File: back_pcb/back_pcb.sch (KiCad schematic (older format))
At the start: 90 parts, among them J1 Conn_01x12, P2 EXPANSION_BOTTOM, P3 EXPANSION_TOP, P4 AUDIO_CONN, P6 ATMEGA_HEADER, P7 EXPANSION_BOTTOM2, P8 JST, P9 USB_A, Q1 IRLML6401, Q2 IRLML6401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

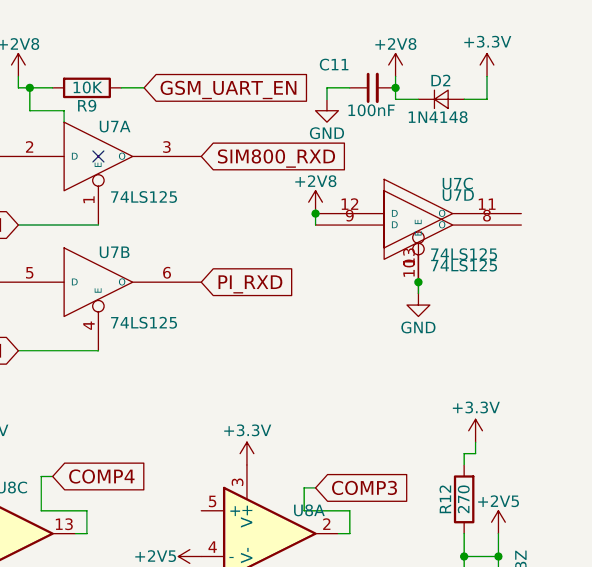
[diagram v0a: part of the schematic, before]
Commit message: Added a 10K resistor pulling up the buffer's unused gate ENs, cleaned up silkscreen
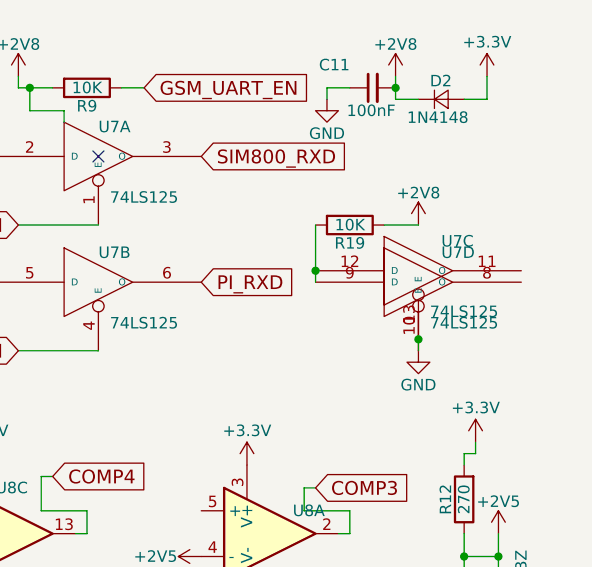
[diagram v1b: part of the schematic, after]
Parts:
- added R19: 10K, common-footprints:R_0805_10K_HandSoldering, symbol R
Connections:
- wire segments 152 -> 153
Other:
- moved on the sheet: U7C, U7D

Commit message: Adjusted JST footprint, connected USB shield to ground, moved some traces and silkscreen labels
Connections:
- no-connect marks 20 -> 19
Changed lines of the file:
@@
 	0    1    1    0
 $EndComp
-NoConn ~ 10850 5350
 $Comp
 L +5V #PWR98
@@
 Text GLabel 6650 6200 0    60   Input ~ 0
 BAT_IN+
-Text Notes 10150 5550 0    60   ~ 0
+Text Notes 10000 5550 0    60   ~ 0
 Full-sized USB \nfemale socket
 $Comp
@@
 Wire Wire Line
 	10500 2700 10650 2700
+$Comp
+L GND #PWR?
+U 1 1 5A8EDCBB
+P 10850 5350
+F 0 "#PWR?" H 10850 5100 50  0001 C CNN
+F 1 "GND" H 10850 5200 50  0000 C CNN
+F 2 "" H 10850 5350 50  0000 C CNN
+F 3 "" H 10850 5350 50  0000 C CNN
+	1    10850 5350
+	1    0    0    -1
+$EndComp
 $EndSCHEMATC

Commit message: Made schematic prettier, fixed the DC-DC FET
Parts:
- D4: value D_Zener -> 5V1
- W1, W4: value TEST_1P -> TXD
- W10: value TEST_1P -> ARX
- W13: value TEST_1P -> ARG
- W14: value TEST_1P -> GND
- W2, W5: value TEST_1P -> RXD
- W29: value TEST_1P -> ADC
- W3: value TEST_1P -> Pi_RST
- W9: value TEST_1P -> ATX
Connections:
- wire segments 153 -> 146
- no-connect marks 19 -> 21
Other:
- note added: "2.6-2.8V for\nthe GSM UART\nbuffer"
- note added: "5050 RGB LED, to be used as a\nflashlight and a notification LED"
- note added: "A TL431-based\nvoltage reference,\nto be used by the\ncomparator."
- note added: "An EEPROM\nfor the hardware version\nidentification, to be programmed\nwith the board version information"
- note added: "Comparators that detect charger\ninput or DC-DC output undervoltage\nThis version will detect back board\noverheating, too"
- note added: "Has two functions:\n1. level-shifting the GSM UART\n2. disabling the GSM UART from\nthe Pi UART until it's needed"
- note added: "Small headers with I2C, 3.3V,\n+5V, one GPIO, VIN and ADC. \nCan be useful for small analog and I2C\nsensors, as well as a dock station port."
- note added: "The UART buffer,\nbased on 74HC125 IC"
- note added: "Unused gates\nof 74HC125"
- note removed: "Small headers with I2C, 3.3V,\n+5V, one GPIO, VIN and ADC. \nCan be useful for small \nanalog and I2C sensors."
- moved on the sheet: C1, C10, C11, C2, C25, C7, D2, D3, D4, JP11, JP12, JP8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

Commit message: Back board changes
Changing 5-pin header footprint to match the RPi 5-header group
Moving the hardware ID EEPROM to I2C0 (ID_SD and ID_SC) pins
Adding pullup on the other I2C pin, as it's required per Pi HAT EEPROM
schematic
Removed TV_OUT pin from Pi Zero footprint
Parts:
- added R20: 10K, common-footprints:R_0805_10K_HandSoldering, symbol R
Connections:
- net labels added: ID_SD
- wire segments 146 -> 148
- no-connect marks 21 -> 20
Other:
- moved on the sheet: R11
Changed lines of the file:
@@
 NoConn ~ 2450 6200
 NoConn ~ 2450 6500
-NoConn ~ 950  4700
 $Comp
 L GND #PWR016
@@
 Text Notes 8950 5950 0    60   ~ 0
 Header with 2 GPIOs\nfor IR receiver \nor transmitter\n(or something else)
-Text GLabel 6600 6900 0    60   Input ~ 0
+Text GLabel 6600 7000 0    60   Input ~ 0
 SCL
 $Comp
 L GND #PWR025
 U 1 1 588A4E65
-P 6600 7100
-F 0 "#PWR025" H 6600 6850 50  0001 C CNN
-F 1 "GND" V 6600 6900 50  0000 C CNN
-F 2 "" H 6600 7100 50  0000 C CNN
-F 3 "" H 6600 7100 50  0000 C CNN
-	1    6600 7100
+P 6600 7200
+F 0 "#PWR025" H 6600 6950 50  0001 C CNN
+F 1 "GND" V 6600 7000 50  0000 C CNN
+F 2 "" H 6600 7200 50  0000 C CNN
+F 3 "" H 6600 7200 50  0000 C CNN
+	1    6600 7200
 	0    1    1    0
 $EndComp
 Text GLabel 5000 6900 2    60   Input ~ 0
 ATMEGA_ADC
-Text GLabel 6600 7000 0    60   Input ~ 0
+Text GLabel 6600 6900 0    60   Input ~ 0
 SDA
 Text Notes 4750 7450 0    60   ~ 0
@@
 	1    0    0    -1
 $EndComp
-Text GLabel 6850 1050 0    60   Input ~ 0
+Text GLabel 6600 1050 0    60   Input ~ 0
 MCP_INT
 $Comp
 L R R11
 U 1 1 58914037
-P 6850 800
-F 0 "R11" V 6930 800 50  0000 C CNN
-F 1 "10K" V 6850 800 50  0000 C CNN
-F 2 "common-footprints:R_0805_10K_HandSoldering" V 6780 800 50  0001 C CNN
-F 3 "" H 6850 800 50  0000 C CNN
-	1    6850 800
+P 6600 800
+F 0 "R11" V 6680 800 50  0000 C CNN
+F 1 "10K" V 6600 800 50  0000 C CNN
+F 2 "common-footprints:R_0805_10K_HandSoldering" V 6530 800 50  0001 C CNN
+F 3 "" H 6600 800 50  0000 C CNN
+	1    6600 800
 	1    0    0    -1
 $EndComp
@@
 	1    0    0    -1
 $EndComp
-Text GLabel 6600 6800 0    60   Input ~ 0
+Text GLabel 6600 7100 0    60   Input ~ 0
 BH_GPIO_1
 Text GLabel 2950 5450 2    60   Input ~ 0
@@
 L +3.3VA #PWR062
 U 1 1 5A853C54
-P 6600 7200
-F 0 "#PWR062" H 6600 7050 50  0001 C CNN
-F 1 "+3.3VA" V 6600 7450 50  0000 C CNN
-F 2 "" H 6600 7200 50  0001 C CNN
-F 3 "" H 6600 7200 50  0001 C CNN
-	1    6600 7200
+P 6600 6800
+F 0 "#PWR062" H 6600 6650 50  0001 C CNN
+F 1 "+3.3VA" V 6600 7050 50  0000 C CNN
+F 2 "" H 6600 6800 50  0001 C CNN
+F 3 "" H 6600 6800 50  0001 C CNN
+	1    6600 6800
 	0    -1   -1   0
 $EndComp
@@
 L +3.3VA #PWR064
 U 1 1 5A856D5E
-P 6850 650
-F 0 "#PWR064" H 6850 500 50  0001 C CNN
-F 1 "+3.3VA" H 6650 750 50  0000 C CNN
-F 2 "" H 6850 650 50  0001 C CNN
-F 3 "" H 6850 650 50  0001 C CNN
-	1    6850 650
+P 6600 650
+F 0 "#PWR064" H 6600 500 50  0001 C CNN
+F 1 "+3.3VA" H 6400 750 50  0000 C CNN
+F 2 "" H 6600 650 50  0001 C CNN
+F 3 "" H 6600 650 50  0001 C CNN
+	1    6600 650
 	1    0    0    -1
 $EndComp
@@
 L +3.3V #PWR073
 U 1 1 5A8624E1
-P 8600 1100
-F 0 "#PWR073" H 8600 950 50  0001 C CNN
-F 1 "+3.3V" H 8600 1250 50  0000 C CNN
-F 2 "" H 8600 1100 50  0000 C CNN
-F 3 "" H 8600 1100 50  0000 C CNN
-	1    8600 1100
-	1    0    0    -1
-$EndComp
-Text GLabel 8250 950  2    60   Input ~ 0
-SDA
-Text GLabel 8250 1050 2    60   Input ~ 0
-SCL
+P 8650 1200
+F 0 "#PWR073" H 8650 1050 50  0001 C CNN
+F 1 "+3.3V" H 8650 1350 50  0000 C CNN
+F 2 "" H 8650 1200 50  0000 C CNN
+F 3 "" H 8650 1200 50  0000 C CNN
+	1    8650 1200
+	-1   0    0    1
+$EndComp
 $Comp
 L GND #PWR074
@@
 	8250 1150 8300 1150
 Wire Wire Line
-	8600 1150 8600 1100
-Wire Wire Line
 	8250 1150 8250 1250
 Connection ~ 8250 1150
@@
 5050 RGB LED, to be used as a\nflashlight and a notification LED
 Wire Wire Line
-	6850 1050 6850 950
+	6600 1050 6600 950
 Wire Wire Line
 	10550 700  10550 750
@@
 Text Notes 10000 3650 0    60   ~ 0
 A TL431-based\nvoltage reference,\nto be used by the\ncomparator.
+Text GLabel 8250 1050 2    60   Input ~ 0
+MCP_INT
+Text GLabel 950  4700 0    60   Input ~ 0
+ID_SD
+Text GLabel 8250 950  2    60   Input ~ 0
+ID_SD
+Wire Wire Line
+	8600 1150 8650 1150
+Wire Wire Line
+	8650 1150 8650 1200
+$Comp
+L R R20
+U 1 1 5AA73F34
+P 6950 800
+F 0 "R20" V 7030 800 50  0000 C CNN
+F 1 "10K" V 6950 800 50  0000 C CNN
+F 2 "common-footprints:R_0805_10K_HandSoldering" V 6880 800 50  0001 C CNN
+F 3 "" H 6950 800 50  0000 C CNN
+	1    6950 800
+	1    0    0    -1
+$EndComp
+$Comp
+L +3.3VA #PWR0110
+U 1 1 5AA7406E
+P 6950 650
+F 0 "#PWR0110" H 6950 500 50  0001 C CNN
+F 1 "+3.3VA" H 6750 750 50  0000 C CNN
+F 2 "" H 6950 650 50  0001 C CNN
+F 3 "" H 6950 650 50  0001 C CNN
+	1    6950 650
+	1    0    0    -1
+$EndComp
+Text GLabel 6950 1050 0    60   Input ~ 0
+ID_SD
+Wire Wire Line
+	6950 1050 6950 950
 $EndSCHEMATC

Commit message: Removed MCP23017 addr jumpers, added fiducials, specified EEPROM model, added power-button-sense circuit, removed battery capacitor
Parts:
- removed C3: 100uF, Capacitors_Tantalum_SMD:CP_Tantalum_Case-B_EIA-3528-21_Hand, symbol C_Small
- removed JP3: A0, common-footprints:GS3_SMALL, symbol JUMPER3
- removed JP4: A1, common-footprints:GS3_SMALL, symbol JUMPER3
- removed JP6: A2, common-footprints:GS3_SMALL, symbol JUMPER3
- added D6: 1N4148, common-footprints:1N4148-D_MiniMELF_Handsoldering, symbol D_Small
- added R21, R22: 270, Resistors_SMD:R_0603_HandSoldering, symbol R
- added R23: 10K, common-footprints:R_0805_10K_HandSoldering, symbol R
- added TP1: FID1, Fiducials:Fiducial_1mm_Dia_2mm_Outer, symbol TEST
- added TP2: FID2, Fiducials:Fiducial_1mm_Dia_2mm_Outer, symbol TEST
- added TP3: FID3, Fiducials:Fiducial_1mm_Dia_2mm_Outer, symbol TEST
- added TP4: FID4, Fiducials:Fiducial_1mm_Dia_2mm_Outer, symbol TEST
- added TP5: FID5, Fiducials:Fiducial_1mm_Dia_2mm_Outer, symbol TEST
- added TP6: FID6, Fiducials:Fiducial_1mm_Dia_2mm_Outer, symbol TEST
- added TP7: FID7, Fiducials:Fiducial_1mm_Dia_2mm_Outer, symbol TEST
- added TP8: FID8, Fiducials:Fiducial_1mm_Dia_2mm_Outer, symbol TEST
- U5: value 24LC16 -> 24C32
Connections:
- wire segments 148 -> 146
- no-connect marks 20 -> 28
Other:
- note added: "JST-PH 2-pin\nbattery connector"
- note removed: "The address pins are \ninterconnected for a default \naddress (tracks can be cut \nand jumpered for custom \naddress)"
- moved on the sheet: P8, R4, U4

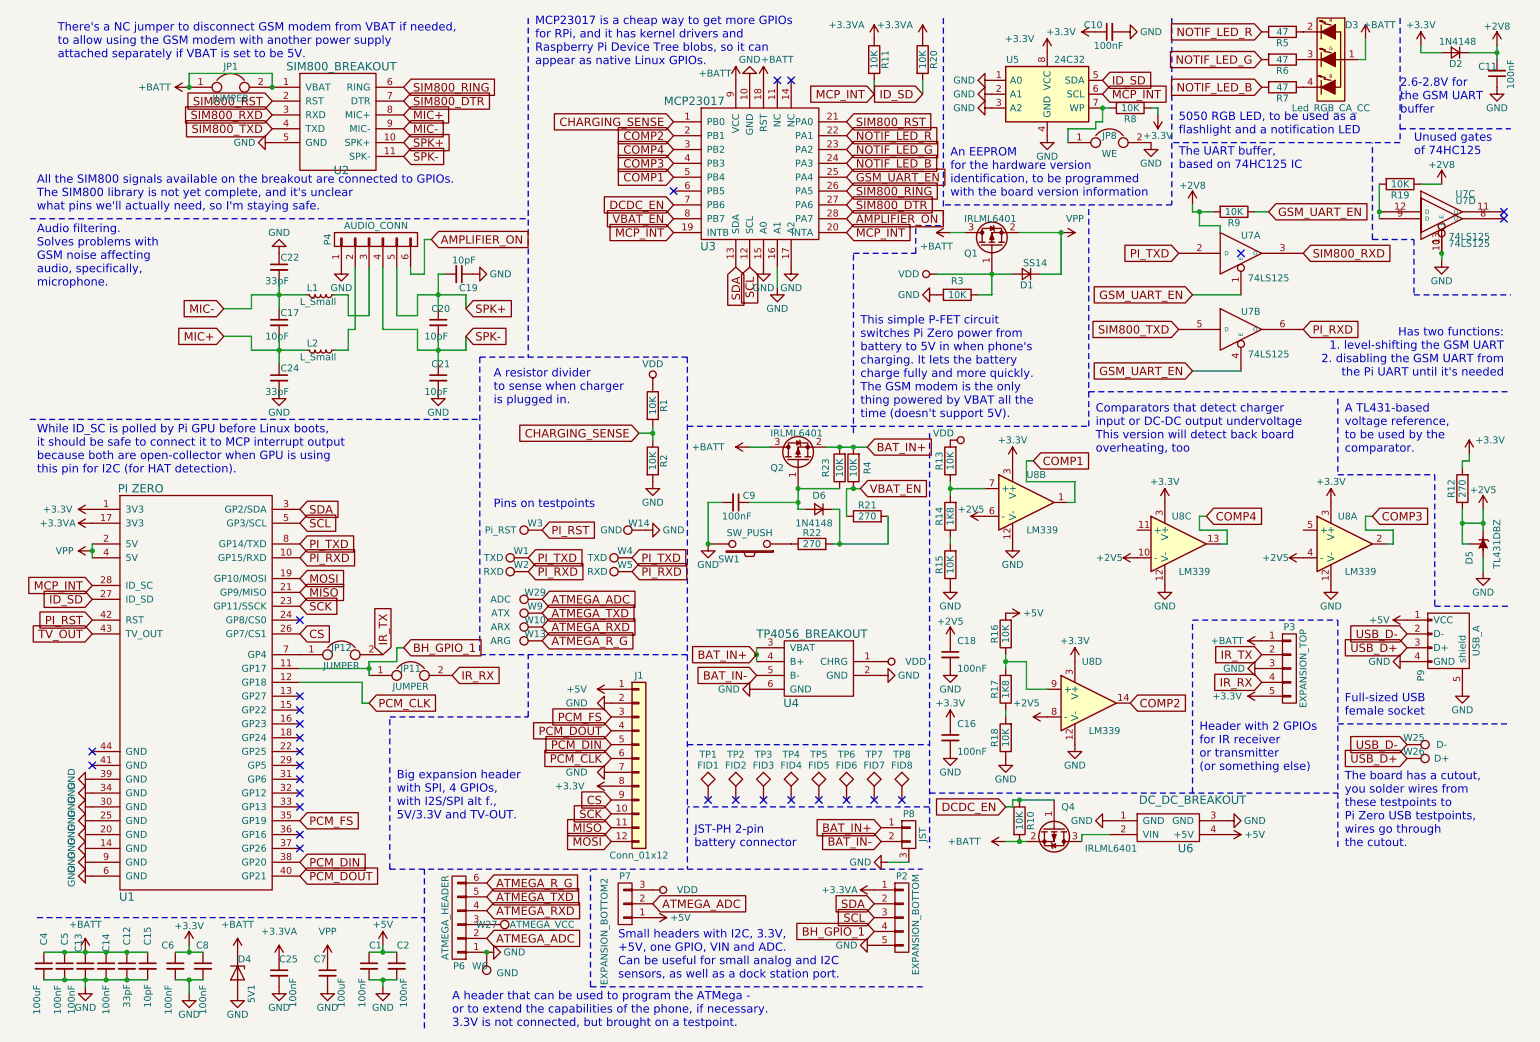
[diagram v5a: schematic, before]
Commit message: Added TP4056 temp sensing, charger-USB switchover and updated the 6-pin connector to have VBAT
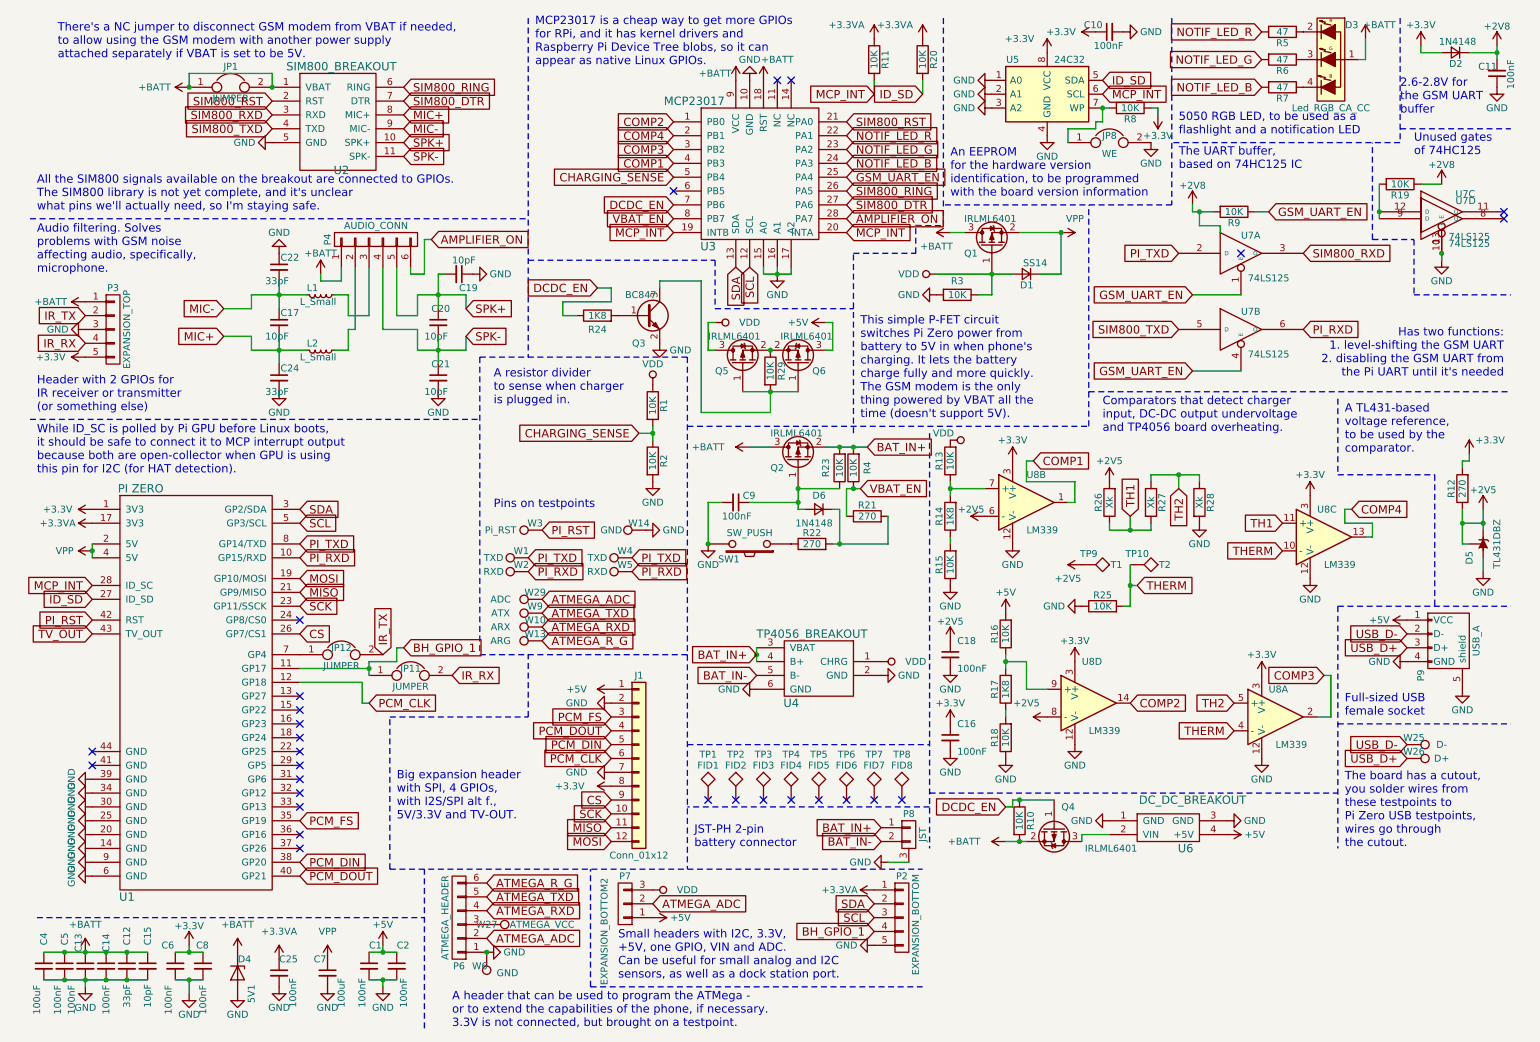
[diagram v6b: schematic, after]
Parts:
- added Q3: BC847, common-footprints:BC847B-SOT-23_Handsoldering, symbol BC847
- added Q5, Q6: IRLML6401, common-footprints:IRLML6401-SOT-23_Handsoldering, symbol Q_PMOS_GSD
- added R24: 1K8, Resistors_SMD:R_0603_HandSoldering, symbol R
- added R25, R29: 10K, common-footprints:R_0805_10K_HandSoldering, symbol R
- added R26, R27, R28: Xk, Resistors_SMD:R_0805_HandSoldering, symbol R
- added TP10: T2, Measurement_Points:Measurement_Point_Round-SMD-Pad_Small, symbol TEST
- added TP9: T1, Measurement_Points:Measurement_Point_Round-SMD-Pad_Small, symbol TEST
- D5: footprint TO_SOT_Packages_SMD:SOT-23 -> TO_SOT_Packages_SMD:SOT-23_Handsoldering
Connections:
- net +2V5: now also R26.2, TP9.1; no longer U8.10 (-), U8.4 (-)
- net +5V: now also Q6.3 (D)
- net +BATT: now also P4.1 (P1)
- net CHARGING_SENSE: now also U3.5 (PB4); no longer U3.1 (PB0)
- net COMP1: now also U3.4 (PB3); no longer U3.5 (PB4)
- net COMP2: now also U3.1 (PB0); no longer U3.2 (PB1)
- net COMP3: now also U3.3 (PB2); no longer U3.4 (PB3)
- net COMP4: now also U3.2 (PB1); no longer U3.3 (PB2)
- net DCDC_EN: now also R24.1
- net GND: now also Q3.2 (E), R25.1, R28.2; no longer P4.1 (P1)
- net VDD: now also Q5.3 (D)
- net TH2: now reaches U8.5 (+)
- net TH2: now also R27.1, R28.1
- net TH1: now reaches U8.11 (+)
- net TH1: now also R26.1, R27.2
- new net: Q3.3 (C), Q5.1 (G), Q6.1 (G), R29.2
- new net: Q5.2 (S), Q6.2 (S), R29.1
- new net: Q3.1 (B), R24.2
- new net THERM: R25.2, TP10.1, U8.10 (-), U8.4 (-)
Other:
- note added: "Audio filtering. Solves\nproblems with GSM noise\naffecting audio, specifically,\nmicrophone."
- note added: "Comparators that detect charger\ninput, DC-DC output undervoltage\nand TP4056 board overheating."
- note added: "Header with 2 GPIOs for\nIR receiver or transmitter\n(or something else)"
- note removed: "Audio filtering.\nSolves problems with \nGSM noise affecting \naudio, specifically,\nmicrophone."
- note removed: "Comparators that detect charger\ninput or DC-DC output undervoltage\nThis version will detect back board\noverheating, too"
- note removed: "Header with 2 GPIOs\nfor IR receiver \nor transmitter\n(or something else)"
- moved on the sheet: P3, U8A, U8C
